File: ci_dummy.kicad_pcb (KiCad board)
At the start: 6 copper layers, 0 parts

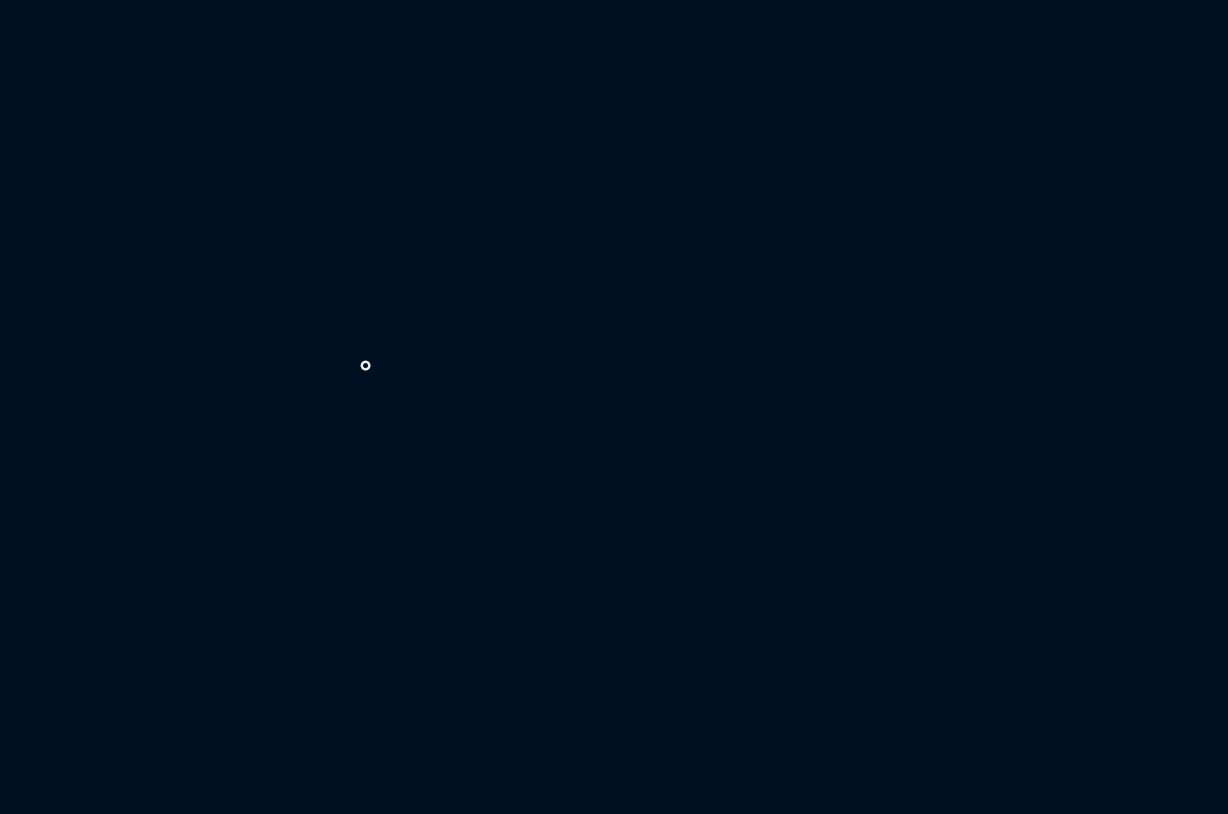
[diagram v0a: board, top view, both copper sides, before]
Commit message: pcb: board outline, update PCB from schematic (10 resistors)
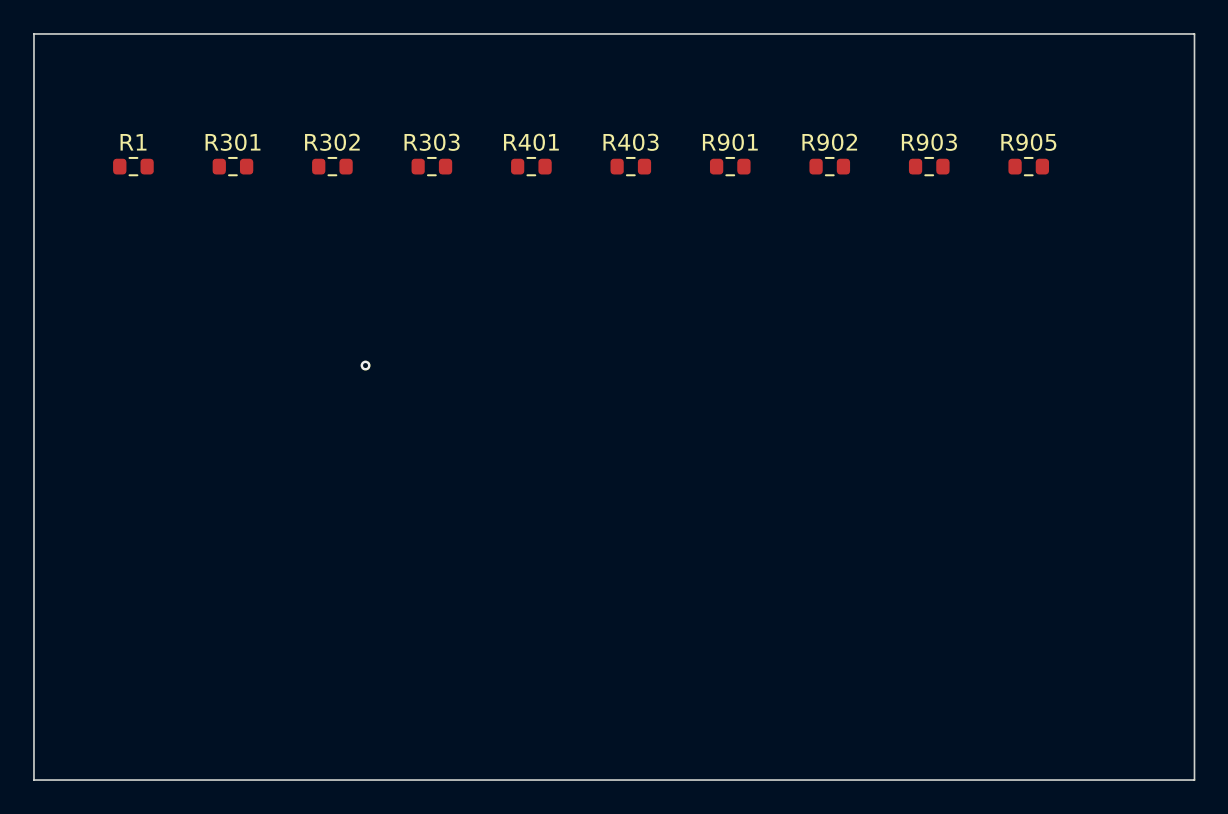
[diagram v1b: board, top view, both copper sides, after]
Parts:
- added R1: 2k2, Resistor_SMD:R_0603_1608Metric, F.Cu at (86.0, 88.0)
- added R301: 10k, Resistor_SMD:R_0603_1608Metric, F.Cu at (92.0, 88.0)
- added R302: 22k, Resistor_SMD:R_0603_1608Metric, F.Cu at (98.0, 88.0)
- added R303: 47k, Resistor_SMD:R_0603_1608Metric, F.Cu at (104.0, 88.0)
- added R401: 4k7, Resistor_SMD:R_0603_1608Metric, F.Cu at (110.0, 88.0)
- added R403: 3k3, Resistor_SMD:R_0603_1608Metric, F.Cu at (116.0, 88.0)
- added R901: 100k, Resistor_SMD:R_0603_1608Metric, F.Cu at (122.0, 88.0)
- added R902: 100k, Resistor_SMD:R_0603_1608Metric, F.Cu at (128.0, 88.0)
- added R903: 1k, Resistor_SMD:R_0603_1608Metric, F.Cu at (134.0, 88.0)
- added R905: 10k, Resistor_SMD:R_0603_1608Metric, F.Cu at (140.0, 88.0)
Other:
- board outline added: 70 x 45 mm

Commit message: Update Outputs (release)
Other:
- board text added: "0.02mm"
- board text added: "0.035mm (1.00oz)"
- board text added: "0.07mm (2.00oz)"
- board text added: "0.18mm"
- board text added: "0.4mm"
- board text added: "B.Mask"
- board text added: "B.Paste"
- board text added: "B.Silkscreen"
- board text added: "Copper"
- board text added: "Core"
- board text added: "Dielectric"
- board text added: "Direct Printing"
- board text added: "F.Mask"
- board text added: "F.Paste"
- board text added: "F.Silkscreen"
- board text added: "FR4"
- board text added: "FR4_7628"
- board text added: "GBR"
- board text added: "Gerber"
- board text added: "L1 (Sig, PWR)"
- board text added: "L2 (GND)"
- board text added: "L3 (Sig, PWR)"
- board text added: "L4 (Sig, PWR)"
- board text added: "L5 (GND)"
- board text added: "L6 (Sig, PWR)"
- board text added: "Layer"
- board text added: "Legend"
- board text added: "Material"
- board text added: "Note: external layer thicknesses are specified after plating"
- board text added: "Paste Mask"
- board text added: "Plane"
- board text added: "Prepreg"
- board text added: "Signal"
- board text added: "Solder Mask"
- board text added: "Solder Resist"
- board text added: "Thickness"
- board text added: "Total thickness: 1.66mm"
- board text added: "Type"

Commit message: dev: no-connects + footprints for R304/R405 before release
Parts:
- added R304: 68k, Resistor_SMD:R_0603_1608Metric, F.Cu at (110.0, 88.0)
- added R405: 150, Resistor_SMD:R_0603_1608Metric, F.Cu at (128.0, 88.0)
- added R906: 33k, Resistor_SMD:R_0603_1608Metric, F.Cu at (98.0, 94.0)
